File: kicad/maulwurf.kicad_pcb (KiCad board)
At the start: 2 copper layers, 63.5 x 70 mm, 17 parts

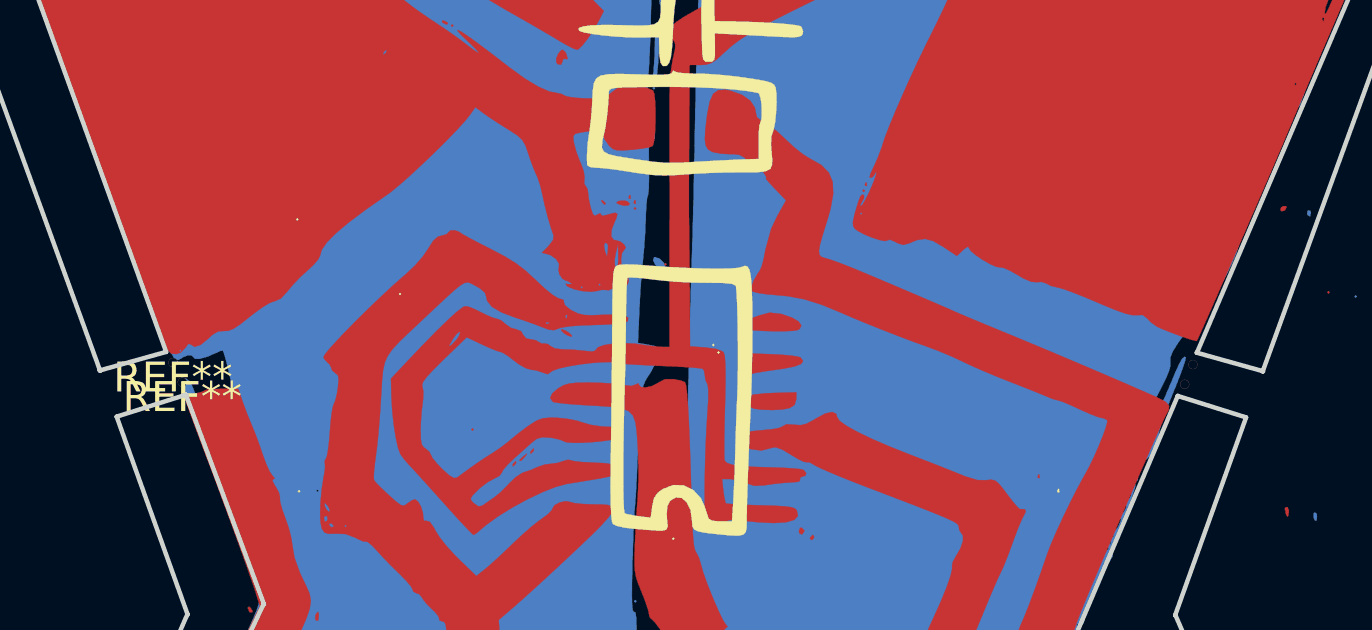
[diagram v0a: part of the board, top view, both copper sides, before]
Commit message: Add some vias to connect up the bottom
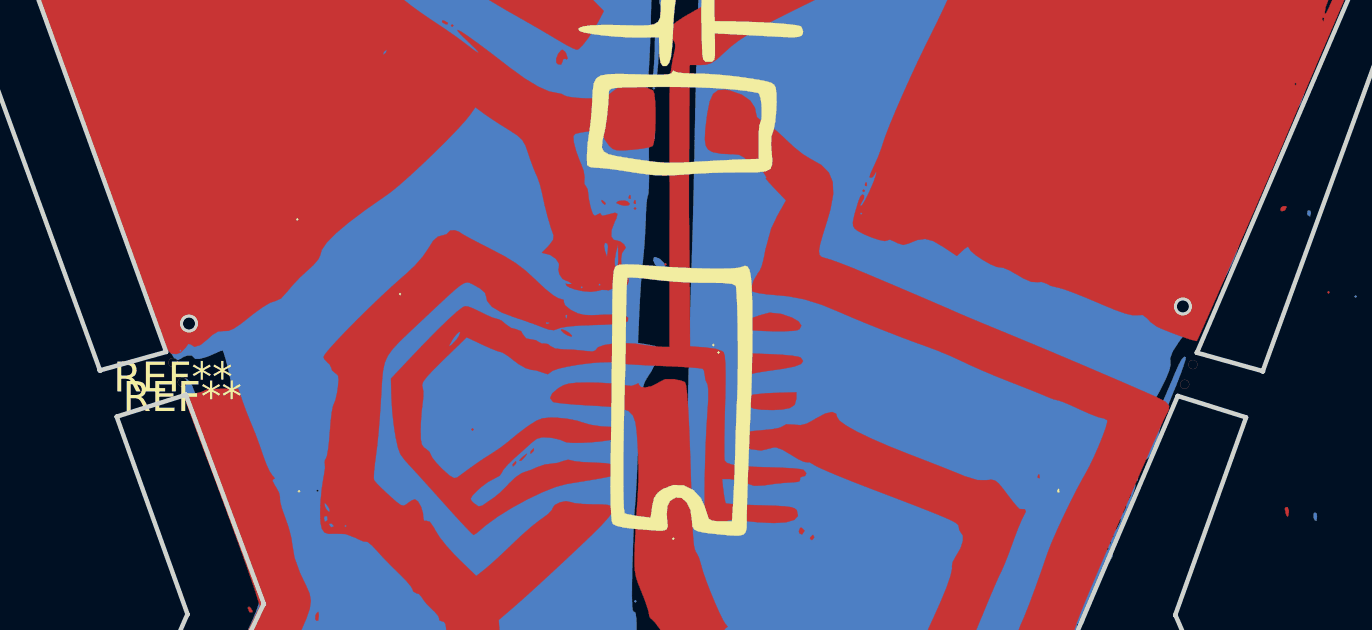
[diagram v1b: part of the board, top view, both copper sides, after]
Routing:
- net (no net): vias 0 -> 2
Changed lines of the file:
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@@
-(kicad_pcb (version 4) (host pcbnew 4.0.7-e2-6376~58~ubuntu16.04.1)
+(kicad_pcb (version 20171130) (host pcbnew 5.0.0-fee4fd1~66~ubuntu16.04.1)
   (general
-    (links 0)
-    (no_connects 0)
-    (area 107.924999 55.664333 171.575001 130.075001)
     (thickness 1.6)
     (drawings 57)
-    (tracks 1)
+    (tracks 3)
     (zones 0)
     (modules 17)
@@
     (visible_elements FFFFFF7F)
     (pcbplotparams
-      (layerselection 0x010f0_80000001)
+      (layerselection 0x010f0_ffffffff)
       (usegerberextensions false)
+      (usegerberattributes false)
+      (usegerberadvancedattributes false)
+      (creategerberjobfile false)
       (excludeedgelayer true)
       (linewidth 0.020000)
@@
       (hpglpennumber 1)
       (hpglpenspeed 20)
-      (hpglpendiameter 15)
-      (hpglpenoverlay 2)
+      (hpglpendiameter 15.000000)
       (psnegative false)
       (psa4output false)
@@
       (drillshape 0)
       (scaleselection 1)
-      (outputdirectory ../gerbers/))
+      (outputdirectory "../gerbers/"))
   )
   (net 0 "")
@@
     (at 163.658 121.284)
     (fp_text reference MASK (at -23.68 -28.5) (layer F.SilkS) hide
-      (effects (font (thickness 0.3)))
+      (effects (font (size 1.524 1.524) (thickness 0.3)))
     )
     (fp_text value Mask (at -22.93 -28.5) (layer F.SilkS) hide
-      (effects (font (thickness 0.3)))
+      (effects (font (size 1.524 1.524) (thickness 0.3)))
     )
     (fp_poly (pts (xy -18.832833 -23.815617) (xy -18.663574 -23.771154) (xy -18.399257 -23.670955) (xy -18.095653 -23.536257)
@@
     (at 163.597 121.129)
     (fp_text reference TOP (at -23.58 -28.59) (layer F.SilkS) hide
-      (effects (font (thickness 0.3)))
+      (effects (font (size 1.524 1.524) (thickness 0.3)))
     )
     (fp_text value Top (at -22.83 -28.59) (layer F.SilkS) hide
-      (effects (font (thickness 0.3)))
+      (effects (font (size 1.524 1.524) (thickness 0.3)))
     )
     (fp_poly (pts (xy -22.743122 -29.684091) (xy -22.353138 -29.547541) (xy -22.067277 -29.348452) (xy -21.911851 -29.108331)
@@
     (at 163.652 121.142 0.2)
     (fp_text reference G*** (at -22.65 -28.47 0.2) (layer F.SilkS) hide
-      (effects (font (thickness 0.3)))
+      (effects (font (size 1.524 1.524) (thickness 0.3)))
     )
     (fp_text value LOGO (at -21.9 -28.47 0.2) (layer F.SilkS) hide
-      (effects (font (thickness 0.3)))
+      (effects (font (size 1.524 1.524) (thickness 0.3)))
     )
     (fp_poly (pts (xy -49.343558 6.560324) (xy -49.343306 6.56235) (xy -49.329479 6.838461) (xy -49.34417 7.07035)
@@
     (at 163.633 121.176 0.9)
     (fp_text reference G*** (at -23.21 -29.7 0.9) (layer F.SilkS) hide
-      (effects (font (thickness 0.3)))
+      (effects (font (size 1.524 1.524) (thickness 0.3)))
     )
     (fp_text value LOGO (at -22.46 -29.7 0.9) (layer F.SilkS) hide
-      (effects (font (thickness 0.3)))
+      (effects (font (size 1.524 1.524) (thickness 0.3)))
     )
     (fp_poly (pts (xy -33.708666 4.039667) (xy -33.751 4.082) (xy -33.793333 4.039667) (xy -33.751 3.997334)
@@
   (gr_line (start 122.06 100.157) (end 114.9 80.4) (layer Edge.Cuts) (width 0.15))
   (segment (start 139.193 98.182) (end 139.193 100.299) (width 0.25) (layer F.Cu) (net 0))
+  (via (at 155.95 98.64) (size 0.6) (drill 0.4) (layers F.Cu B.Cu) (net 0))
+  (via (at 122.82 99.21) (size 0.6) (drill 0.4) (layers F.Cu B.Cu) (net 0))
   (zone (net 0) (net_name "") (layer B.Mask) (hatch edge 0.508)
     (connect_pads (clearance 0.508))

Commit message: Remove frame
fixes #3
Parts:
- removed REF** (x13): hole, footprints:hole
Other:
- board size 63.5 x 70 mm -> 52.1 x 63.8 mm

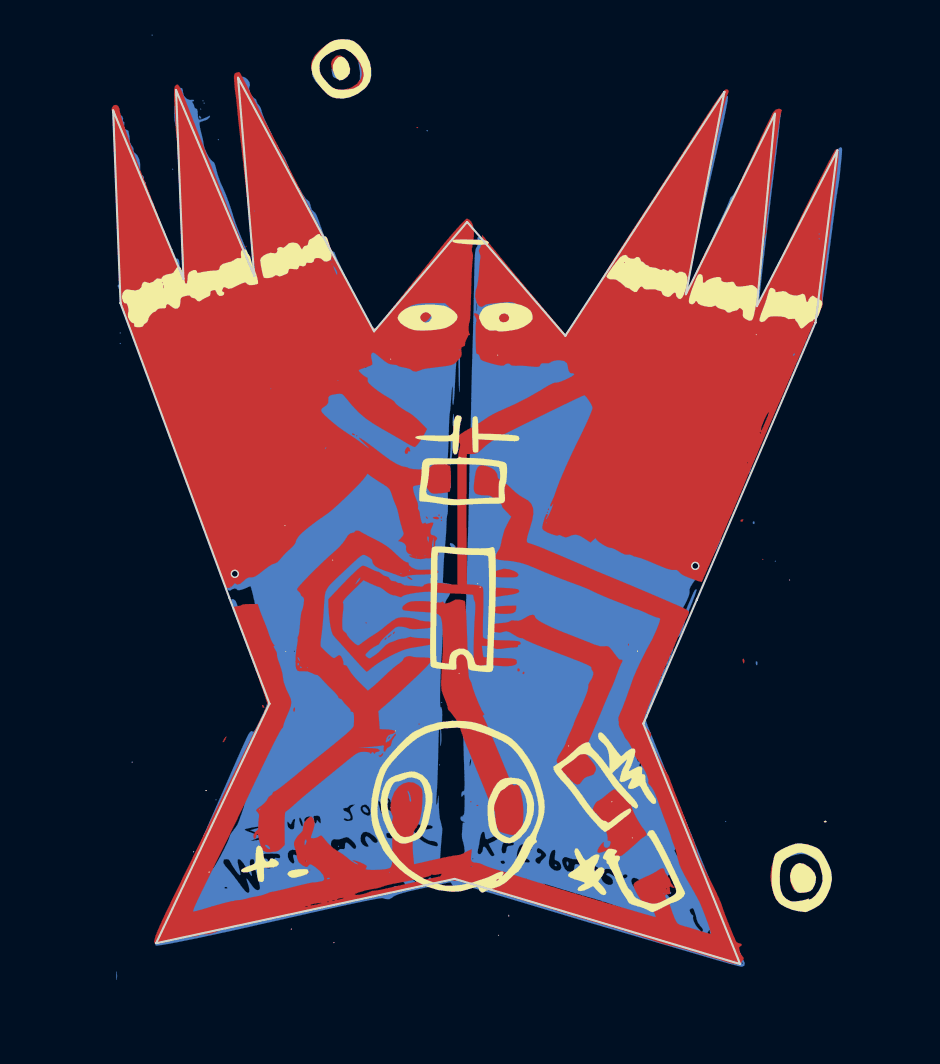
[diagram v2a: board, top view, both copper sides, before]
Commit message: Re-do bottom copper layer
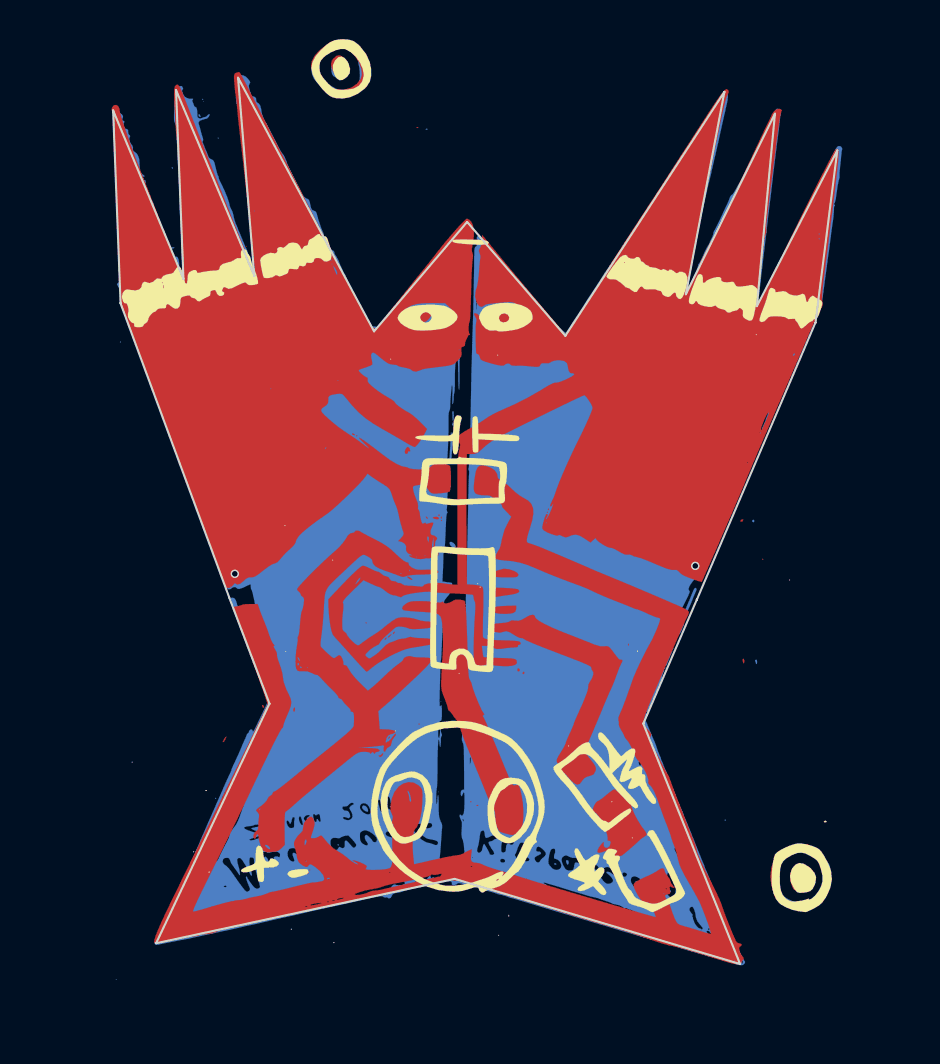
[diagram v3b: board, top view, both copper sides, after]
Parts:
- moved G*** 36.4 mm to (140.9, 92.7)

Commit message: Turn the board 180 degrees
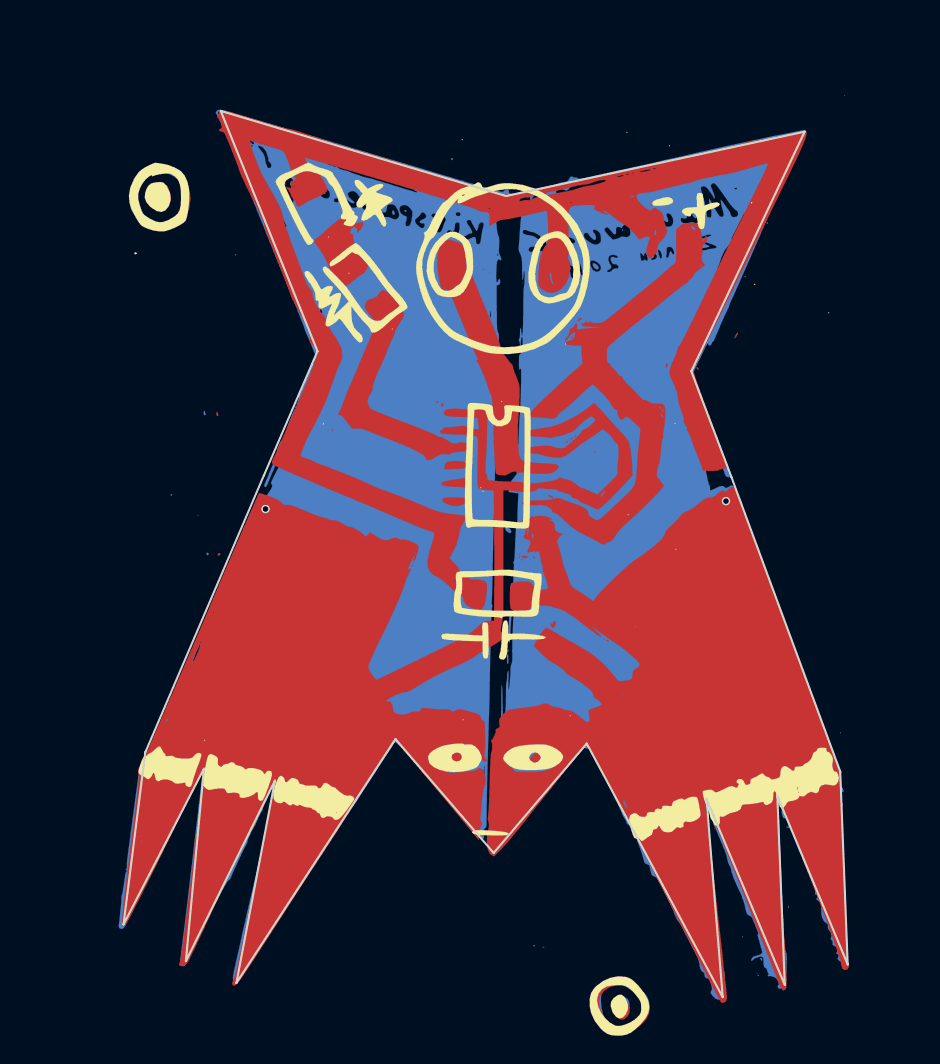
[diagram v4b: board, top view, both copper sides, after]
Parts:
- moved MASK 67.7 mm to (117.3, 71.9), turned to 180 degrees
- moved G*** 67.5 mm to (117.3, 72.0), turned to 180.9 degrees
- moved TOP 67.4 mm to (117.4, 72.1), turned to 180 degrees
- moved G*** 7.94 mm to (140.1, 100.5), turned to 180.2 degrees
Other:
- outline, holes or cut-outs redrawn
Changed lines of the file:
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@@
     (pad_to_mask_clearance 0.2)
     (aux_axis_origin 0 0)
-    (visible_elements FFFFFF7F)
+    (visible_elements FFFFFFFF)
     (pcbplotparams
       (layerselection 0x010f0_ffffffff)
@@
   )
   (module footprints:bottom (layer F.Cu)
-    (at 140.92 92.65 0.2)
-    (fp_text reference G*** (at -22.65 -28.47 0.2) (layer F.SilkS) hide
+    (at 140.06 100.54 180.2)
+    (fp_text reference G*** (at -22.65 -28.47 180.2) (layer F.SilkS) hide
       (effects (font (size 1.524 1.524) (thickness 0.3)))
     )
-    (fp_text value LOGO (at -21.9 -28.47 0.2) (layer F.SilkS) hide
+    (fp_text value LOGO (at -21.9 -28.47 180.2) (layer F.SilkS) hide
       (effects (font (size 1.524 1.524) (thickness 0.3)))
     )
@@
   )
   (module footprints:mask (layer F.Cu)
-    (at 163.658 121.284)
-    (fp_text reference MASK (at -23.68 -28.5) (layer F.SilkS) hide
+    (at 117.322 71.906 180)
+    (fp_text reference MASK (at -23.68 -28.5 180) (layer F.SilkS) hide
       (effects (font (size 1.524 1.524) (thickness 0.3)))
     )
-    (fp_text value Mask (at -22.93 -28.5) (layer F.SilkS) hide
+    (fp_text value Mask (at -22.93 -28.5 180) (layer F.SilkS) hide
       (effects (font (size 1.524 1.524) (thickness 0.3)))
     )
@@
   )
   (module footprints:top (layer F.Cu)
-    (at 163.597 121.129)
-    (fp_text reference TOP (at -23.58 -28.59) (layer F.SilkS) hide
+    (at 117.383 72.061 180)
+    (fp_text reference TOP (at -23.58 -28.59 180) (layer F.SilkS) hide
       (effects (font (size 1.524 1.524) (thickness 0.3)))
     )
-    (fp_text value Top (at -22.83 -28.59) (layer F.SilkS) hide
+    (fp_text value Top (at -22.83 -28.59 180) (layer F.SilkS) hide
       (effects (font (size 1.524 1.524) (thickness 0.3)))
     )
@@
   )
   (module footprints:silkscreen (layer F.Cu)
-    (at 163.633 121.176 0.9)
-    (fp_text reference G*** (at -23.21 -29.7 0.9) (layer F.SilkS) hide
+    (at 117.347 72.014 180.9)
+    (fp_text reference G*** (at -23.21 -29.7 180.9) (layer F.SilkS) hide
       (effects (font (size 1.524 1.524) (thickness 0.3)))
     )
-    (fp_text value LOGO (at -22.46 -29.7 0.9) (layer F.SilkS) hide
+    (fp_text value LOGO (at -22.46 -29.7 180.9) (layer F.SilkS) hide
       (effects (font (size 1.524 1.524) (thickness 0.3)))
     )
@@
       (xy -32.213849 -59.695039) (xy -31.985009 -59.594131)) (layer F.SilkS) (width 0.01))
   )
-  (gr_line (start 166.169 68.752) (end 164.6 81.15) (layer Edge.Cuts) (width 0.15))
-  (gr_line (start 139.6 128) (end 140.5 128) (layer F.Mask) (width 0.2))
-  (gr_line (start 139.6 128) (end 140.4 128) (layer F.Mask) (width 0.2))
-  (gr_line (start 140.4 128) (end 140.5 128) (layer F.Mask) (width 0.2))
-  (gr_line (start 125.322 108.571) (end 122.41 100.9) (layer Edge.Cuts) (width 0.15))
-  (gr_line (start 152.216 109.984) (end 156.07 101.05) (layer Edge.Cuts) (width 0.15))
-  (gr_line (start 117.158 125.793) (end 125.312 108.551) (layer Edge.Cuts) (width 0.15))
-  (gr_line (start 138.64 121.16) (end 117.158 125.793) (layer Edge.Cuts) (width 0.15))
-  (gr_line (start 159.174 127.286) (end 138.64 121.16) (layer Edge.Cuts) (width 0.15))
-  (gr_line (start 152.205 109.981) (end 159.174 127.286) (layer Edge.Cuts) (width 0.15))
-  (gr_line (start 164.6 81.13) (end 156.06 101.08) (layer Edge.Cuts) (width 0.15))
-  (gr_line (start 160.381 79.955) (end 166.169 68.752) (layer Edge.Cuts) (width 0.15))
-  (gr_line (start 161.683 66.106) (end 160.381 79.955) (layer Edge.Cuts) (width 0.15))
-  (gr_line (start 155.273 79.099) (end 161.683 66.106) (layer Edge.Cuts) (width 0.15))
-  (gr_line (start 158.048 64.534) (end 155.273 79.099) (layer Edge.Cuts) (width 0.15))
-  (gr_line (start 146.601 82.086) (end 158.048 64.534) (layer Edge.Cuts) (width 0.15))
-  (gr_line (start 139.545 73.904) (end 146.601 82.086) (layer Edge.Cuts) (width 0.15))
-  (gr_line (start 132.839 81.766) (end 139.532 73.896) (layer Edge.Cuts) (width 0.15))
-  (gr_line (start 123.054 63.516) (end 132.839 81.766) (layer Edge.Cuts) (width 0.15))
-  (gr_line (start 124.22 77.774) (end 123.054 63.516) (layer Edge.Cuts) (width 0.15))
-  (gr_line (start 118.59 64.406) (end 124.22 77.774) (layer Edge.Cuts) (width 0.15))
-  (gr_line (start 119.124 77.993) (end 118.59 64.406) (layer Edge.Cuts) (width 0.15))
-  (gr_line (start 114.062 65.872) (end 119.124 77.993) (layer Edge.Cuts) (width 0.15))
-  (gr_line (start 114.6 79.75) (end 114.062 65.872) (layer Edge.Cuts) (width 0.15))
-  (gr_line (start 122.42 100.92) (end 114.59 79.73) (layer Edge.Cuts) (width 0.15))
-  (segment (start 139.193 98.182) (end 139.193 100.299) (width 0.25) (layer F.Cu) (net 0))
-  (via (at 155.95 98.64) (size 0.6) (drill 0.4) (layers F.Cu B.Cu) (net 0))
-  (via (at 122.82 99.21) (size 0.6) (drill 0.4) (layers F.Cu B.Cu) (net 0))
-  (zone (net 0) (net_name "") (layer B.Mask) (hatch edge 0.508)
-    (connect_pads (clearance 0.508))
-    (min_thickness 0.254)
-    (fill yes (arc_segments 16) (thermal_gap 0.508) (thermal_bridge_width 0.508))
-    (polygon
-      (pts
-        (xy 112.5 62.5) (xy 115.5 128) (xy 169 128) (xy 167.5 64.5) (xy 115.5 62.5)
-      )
-    )
-  )
+  (gr_line (start 114.811 124.438) (end 116.38 112.04) (layer Edge.Cuts) (width 0.15))
+  (gr_line (start 141.38 65.19) (end 140.48 65.19) (layer F.Mask) (width 0.2))
+  (gr_line (start 141.38 65.19) (end 140.58 65.19) (layer F.Mask) (width 0.2))
+  (gr_line (start 140.58 65.19) (end 140.48 65.19) (layer F.Mask) (width 0.2))
+  (gr_line (start 155.658 84.619) (end 158.57 92.29) (layer Edge.Cuts) (width 0.15))
+  (gr_line (start 128.764 83.206) (end 124.91 92.14) (layer Edge.Cuts) (width 0.15))
+  (gr_line (start 163.822 67.397) (end 155.668 84.639) (layer Edge.Cuts) (width 0.15))
+  (gr_line (start 142.34 72.03) (end 163.822 67.397) (layer Edge.Cuts) (width 0.15))
+  (gr_line (start 121.806 65.904) (end 142.34 72.03) (layer Edge.Cuts) (width 0.15))
+  (gr_line (start 128.775 83.209) (end 121.806 65.904) (layer Edge.Cuts) (width 0.15))
+  (gr_line (start 116.38 112.06) (end 124.92 92.11) (layer Edge.Cuts) (width 0.15))
+  (gr_line (start 120.599 113.235) (end 114.811 124.438) (layer Edge.Cuts) (width 0.15))
+  (gr_line (start 119.297 127.084) (end 120.599 113.235) (layer Edge.Cuts) (width 0.15))
+  (gr_line (start 125.707 114.091) (end 119.297 127.084) (layer Edge.Cuts) (width 0.15))
+  (gr_line (start 122.932 128.656) (end 125.707 114.091) (layer Edge.Cuts) (width 0.15))
+  (gr_line (start 134.379 111.104) (end 122.932 128.656) (layer Edge.Cuts) (width 0.15))
+  (gr_line (start 141.435 119.286) (end 134.379 111.104) (layer Edge.Cuts) (width 0.15))
+  (gr_line (start 148.141 111.424) (end 141.448 119.294) (layer Edge.Cuts) (width 0.15))
+  (gr_line (start 157.926 129.674) (end 148.141 111.424) (layer Edge.Cuts) (width 0.15))
+  (gr_line (start 156.76 115.416) (end 157.926 129.674) (layer Edge.Cuts) (width 0.15))
+  (gr_line (start 162.39 128.784) (end 156.76 115.416) (layer Edge.Cuts) (width 0.15))
+  (gr_line (start 161.856 115.197) (end 162.39 128.784) (layer Edge.Cuts) (width 0.15))
+  (gr_line (start 166.918 127.318) (end 161.856 115.197) (layer Edge.Cuts) (width 0.15))
+  (gr_line (start 166.38 113.44) (end 166.918 127.318) (layer Edge.Cuts) (width 0.15))
+  (gr_line (start 158.56 92.27) (end 166.39 113.46) (layer Edge.Cuts) (width 0.15))
+  (segment (start 141.787 95.008) (end 141.787 92.891) (width 0.25) (layer F.Cu) (net 0))
+  (via (at 125.03 94.55) (size 0.6) (drill 0.4) (layers F.Cu B.Cu) (net 0))
+  (via (at 158.16 93.98) (size 0.6) (drill 0.4) (layers F.Cu B.Cu) (net 0))
 )
